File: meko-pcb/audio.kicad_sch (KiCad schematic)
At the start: 29 parts, among them IC4 ES9218PQ, J4 SJ2-35954B-SMT-TR, Y1 ECS-2520SMV-500-GP-TR

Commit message: component selection
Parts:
- IC4: Manufacturer_Part_Number ES9218PQ -> (none); Mfr. No. (none) -> ES9218PQ
- J4: Mfr. No. (none) -> SJ2-35954B-SMT-TR
- R27, R33, R35: Mfr. No. (none) -> CRCW040210K0FKED
- R28, R29: Mfr. No. (none) -> RC0402FR-0747KL
- Y1: Manufacturer_Part_Number ECS-2520SMV-500-GP-TR -> (none); Mfr. No. (none) -> ECS-2520SMV-500-GP-TR
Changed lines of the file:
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@@
+			)
+		)
+		(property "Mfr. No." "RC0402FR-0747KL"
+			(at 146.05 39.37 90)
+			(effects
+				(font
+					(size 1.27 1.27)
+				)
+				(hide yes)
 			)
 		)
@@
 			)
 		)
+		(property "Mfr. No." "CRCW040210K0FKED"
+			(at 21.59 132.08 0)
+			(effects
+				(font
+					(size 1.27 1.27)
+				)
+				(hide yes)
+			)
+		)
 		(pin "2"
 		)
@@
 		(property "Description" "Resistor"
 			(at 146.05 45.72 0)
+			(effects
+				(font
+					(size 1.27 1.27)
+				)
+				(hide yes)
+			)
+		)
+		(property "Mfr. No." "RC0402FR-0747KL"
+			(at 146.05 45.72 90)
 			(effects
 				(font
@@
 			)
 		)
+		(property "Mfr. No." " SJ2-35954B-SMT-TR "
+			(at 60.96 129.54 0)
+			(effects
+				(font
+					(size 1.27 1.27)
+				)
+				(hide yes)
+			)
+		)
 		(pin "R1"
 		)
@@
 			)
 		)
-		(property "Manufacturer_Part_Number" "ECS-2520SMV-500-GP-TR"
-			(at 71.12 680.01 0)
-			(effects
-				(font
-					(size 1.27 1.27)
-				)
-				(justify left top)
-				(hide yes)
-			)
-		)
 		(property "Mouser Part Number" "520-2520SMV-500-GP-T"
 			(at 71.12 780.01 0)
@@
 				)
 				(justify left top)
+				(hide yes)
+			)
+		)
+		(property "Mfr. No." "ECS-2520SMV-500-GP-TR"
+			(at 36.83 85.09 0)
+			(effects
+				(font
+					(size 1.27 1.27)
+				)
 				(hide yes)
 			)
@@
 			)
 		)
-		(property "Manufacturer_Part_Number" "ES9218PQ"
-			(at 149.86 666.04 0)
-			(effects
-				(font
-					(size 1.27 1.27)
-				)
-				(justify left top)
-				(hide yes)
-			)
-		)
 		(property "Mouser Part Number" "460-ES9218PQ"
 			(at 149.86 766.04 0)
@@
 			)
 		)
+		(property "Mfr. No." "ES9218PQ"
+			(at 113.03 83.82 0)
+			(effects
+				(font
+					(size 1.27 1.27)
+				)
+				(hide yes)
+			)
+		)
 		(pin "6"
 		)
@@
 		(property "Description" "Resistor"
 			(at 124.46 36.83 0)
+			(effects
+				(font
+					(size 1.27 1.27)
+				)
+				(hide yes)
+			)
+		)
+		(property "Mfr. No." "CRCW040210K0FKED"
+			(at 124.46 36.83 90)
 			(effects
 				(font
@@
 			(at 35.56 92.71 0)
 			(effects
+				(font
+					(size 1.27 1.27)
+				)
+				(hide yes)
+			)
+		)
+		(property "Mfr. No." "CRCW040210K0FKED"
+			(at 35.56 92.71 0)
+			(effects

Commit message: picked MPNs
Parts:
- C41, C43, C44, C45, C52: MPN (none) -> CL05A105KO5NNNC
- C42: MPN (none) -> CL10A226MQ8NRNC
- C46, C47, C48, C49, C50: MPN (none) -> CL05A475KP5NRNC
- C51: MPN (none) -> CL05A225KO5NQNC
- C53, C54, C55, C56: MPN (none) -> CL05B222KB5NNNC
- D10, D11, D12, D9: MPN (none) -> CD0201-T2.0LC; Mfr. No. CD0201-T2.0LC -> (none)
- IC4: MPN (none) -> ES9218PQ; Mfr. No. ES9218PQ -> (none); Mouser Part Number 460-ES9218PQ -> (none); Mouser Price/Stock https://www.mouser.co.uk/ProductDetail/ESS-Technology/ES921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 -> (none)
- J4: MPN (none) -> SJ2-35954B-SMT-TR; Mfr. No. SJ2-35954B-SMT-TR -> (none)
- R27, R33, R35: MPN (none) -> CRCW040210K0FKED; Mfr. No. CRCW040210K0FKED -> (none)
- R28, R29: MPN (none) -> RC0402FR-0747KL; Mfr. No. RC0402FR-0747KL -> (none)
- Y1: MPN (none) -> ECS-2520SMV-500-GP-TR; Mfr. No. ECS-2520SMV-500-GP-TR -> (none); Mouser Part Number 520-2520SMV-500-GP-T -> (none); Mouser Price/Stock https://www.mouser.co.uk/ProductDetail/ECS/ECS-2520SMV-500-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 -> (none)
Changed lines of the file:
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@@
 			)
 		)
+		(property "MPN" "CL05B222KB5NNNC"
+			(at 168.91 99.06 90)
+			(effects
+				(font
+					(size 1.27 1.27)
+				)
+				(hide yes)
+			)
+		)
 		(pin "1"
 		)
@@
 			)
 		)
+		(property "MPN" "CL05B222KB5NNNC"
+			(at 104.14 106.68 0)
+			(effects
+				(font
+					(size 1.27 1.27)
+				)
+				(hide yes)
+			)
+		)
 		(pin "1"
 		)
@@
 			)
 		)
-		(property "Mfr. No." "RC0402FR-0747KL"
+		(property "MPN" "RC0402FR-0747KL"
 			(at 146.05 39.37 90)
 			(effects
@@
 			)
 		)
-		(property "Mfr. No." " CD0201-T2.0LC "
+		(property "MPN" " CD0201-T2.0LC "
 			(at 39.37 147.32 90)
 			(effects
@@
 			)
 		)
+		(property "MPN" "CL05A105KO5NNNC"
+			(at 128.27 142.24 0)
+			(effects
+				(font
+					(size 1.27 1.27)
+				)
+				(hide yes)
+			)
+		)
 		(pin "1"
 		)
@@
 			)
 		)
+		(property "MPN" "CL05A105KO5NNNC"
+			(at 45.72 26.67 0)
+			(effects
+				(font
+					(size 1.27 1.27)
+				)
+				(hide yes)
+			)
+		)
 		(pin "1"
 		)
@@
 			)
 		)
+		(property "MPN" "CL05A105KO5NNNC"
+			(at 168.91 73.66 90)
+			(effects
+				(font
+					(size 1.27 1.27)
+				)
+				(hide yes)
+			)
+		)
 		(pin "1"
 		)
@@
 			)
 		)
+		(property "MPN" "CL05A105KO5NNNC"
+			(at 58.42 26.67 0)
+			(effects
+				(font
+					(size 1.27 1.27)
+				)
+				(hide yes)
+			)
+		)
 		(pin "1"
 		)
@@
 			)
 		)
-		(property "Mfr. No." "CRCW040210K0FKED"
+		(property "MPN" "CRCW040210K0FKED"
 			(at 21.59 132.08 0)
 			(effects
@@
 			)
 		)
-		(property "Mfr. No." "RC0402FR-0747KL"
+		(property "MPN" "RC0402FR-0747KL"
 			(at 146.05 45.72 90)
 			(effects
@@
 			)
 		)
+		(property "MPN" "CL05A105KO5NNNC"
+			(at 147.32 25.4 90)
+			(effects
+				(font
+					(size 1.27 1.27)
+				)
+				(hide yes)
+			)
+		)
 		(pin "2"
 		)
@@
 			)
 		)
+		(property "MPN" "CL05B222KB5NNNC"
+			(at 166.37 106.68 0)
+			(effects
+				(font
+					(size 1.27 1.27)
+				)
+				(hide yes)
+			)
+		)
 		(pin "1"
 		)
@@
 			)
 		)
+		(property "MPN" "CL05A475KP5NRNC"
+			(at 45.72 52.07 0)
+			(effects
+				(font
+					(size 1.27 1.27)
+				)
+				(hide yes)
+			)
+		)
 		(pin "1"
 		)
@@
 			)
 		)
-		(property "Mfr. No." " SJ2-35954B-SMT-TR "
+		(property "MPN" " SJ2-35954B-SMT-TR "
 			(at 60.96 129.54 0)
 			(effects
@@
 			)
 		)
+		(property "MPN" "CL05A475KP5NRNC"
+			(at 21.59 52.07 0)
+			(effects
+				(font
+					(size 1.27 1.27)
+				)
+				(hide yes)
+			)
+		)
 		(pin "1"
 		)
@@
 			)
 		)
-		(property "Mouser Part Number" "520-2520SMV-500-GP-T"
-			(at 71.12 780.01 0)
-			(effects
-				(font
-					(size 1.27 1.27)
-				)
-				(justify left top)
-				(hide yes)
-			)
-		)
-		(property "Mouser Price/Stock" "https://www.mouser.co.uk/ProductDetail/ECS/ECS-2520SMV-500-GP-TR?qs=XeJtXLiO41S1fNQUYV715g%3D%3D"
-			(at 71.12 880.01 0)
-			(effects
-				(font
-					(size 1.27 1.27)
-				)
-				(justify left top)
-				(hide yes)
-			)
-		)
 		(property "Arrow Part Number" "ECS-2520SMV-500-GP-TR"
 			(at 71.12 980.01 0)
@@
 			)
 		)
-		(property "Mfr. No." "ECS-2520SMV-500-GP-TR"
+		(property "MPN" "ECS-2520SMV-500-GP-TR"
 			(at 36.83 85.09 0)
 			(effects
@@
 			)
 		)
-		(property "Mouser Part Number" "460-ES9218PQ"
-			(at 149.86 766.04 0)
-			(effects
-				(font
-					(size 1.27 1.27)
-				)
-				(justify left top)
-				(hide yes)
-			)
-		)
-		(property "Mouser Price/Stock" "https://www.mouser.co.uk/ProductDetail/ESS-Technology/ES9218PQ?qs=sPbYRqrBIVkIKXrxpjKBFg%3D%3D"
-			(at 149.86 866.04 0)
-			(effects
-				(font
-					(size 1.27 1.27)
-				)
-				(justify left top)
-				(hide yes)
-			)
-		)
 		(property "Arrow Part Number" ""
 			(at 149.86 966.04 0)
@@
 			)
 		)
-		(property "Mfr. No." "ES9218PQ"
+		(property "MPN" "ES9218PQ"
 			(at 113.03 83.82 0)
 			(effects
@@
 			)
 		)
+		(property "MPN" "CL05A475KP5NRNC"
+			(at 57.15 52.07 0)
+			(effects
+				(font
+					(size 1.27 1.27)
+				)
+				(hide yes)
+			)
+		)
 		(pin "1"
 		)
@@
 			)
 		)
-		(property "Mfr. No." "CRCW040210K0FKED"
+		(property "MPN" "CRCW040210K0FKED"
 			(at 124.46 36.83 90)
 			(effects
@@
 			)
 		)
+		(property "MPN" "CL05A225KO5NQNC"
+			(at 168.91 68.58 90)
+			(effects
+				(font
+					(size 1.27 1.27)
+				)
+				(hide yes)
+			)
+		)
 		(pin "1"
 		)
@@
 			)
 		)
-		(property "Mfr. No." " CD0201-T2.0LC "
+		(property "MPN" " CD0201-T2.0LC "
 			(at 44.45 147.32 90)
 			(effects
@@
 			)
 		)
-		(property "Mfr. No." " CD0201-T2.0LC "
+		(property "MPN" " CD0201-T2.0LC "
 			(at 49.53 147.32 90)
 			(effects
@@
 			)
 		)
-		(property "Mfr. No." "CRCW040210K0FKED"
+		(property "MPN" "CRCW040210K0FKED"
 			(at 35.56 92.71 0)
 			(effects
@@
 			)
 		)
+		(property "MPN" "CL05A475KP5NRNC"
+			(at 71.12 26.67 0)
+			(effects
+				(font
+					(size 1.27 1.27)
+				)
+				(hide yes)
+			)
+		)
 		(pin "1"
 		)
@@
 			)
 		)
+		(property "MPN" "CL05B222KB5NNNC"
+			(at 95.25 99.06 90)
+			(effects
+				(font
+					(size 1.27 1.27)
+				)
+				(hide yes)
+			)
+		)
 		(pin "1"
 		)
@@
 			)
 		)
-		(property "Mfr. No." " CD0201-T2.0LC "
+		(property "MPN" " CD0201-T2.0LC "
 			(at 54.61 147.32 90)
 			(effects
@@
 			)
 		)
+		(property "MPN" "CL10A226MQ8NRNC"
+			(at 121.92 142.24 0)
+			(effects
+				(font
+					(size 1.27 1.27)
+				)
+				(hide yes)
+			)
+		)
 		(pin "1"
 		)
@@
 			(at 34.29 52.07 0)
 			(effects
+				(font
+					(size 1.27 1.27)
+				)
+				(hide yes)
+			)
+		)
+		(property "MPN" "CL05A475KP5NRNC"
+			(at 34.29 52.07 0)
+			(effects

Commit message: small changes, readme updates
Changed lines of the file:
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@@
 		(dnp no)
 		(property "Reference" "IC4"
-			(at 112.522 72.136 0)
+			(at 99.06 67.31 0)
 			(effects
 				(font
@@
 		)
 		(property "Value" "ES9218PQ"
-			(at 112.522 74.676 0)
+			(at 99.06 69.85 0)
 			(effects
 				(font

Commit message: readme updates, removed unused fileds form kicad
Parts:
- IC4: Height 0.8 -> (none); Manufacturer_Name ESS Technology -> (none)
- Y1: Arrow Part Number ECS-2520SMV-500-GP-TR -> (none); Arrow Price/Stock https://www.arrow.com/en/products/ecs-2520smv-500-gp-tr/ecs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 -> (none); Height 0.9 -> (none); Manufacturer_Name ECS -> (none)
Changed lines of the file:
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@@
-			)
-		)
-		(property "Height" "0.9"
-			(at 71.12 480.01 0)
-			(effects
-				(font
-					(size 1.27 1.27)
-				)
-				(justify left top)
-				(hide yes)
-			)
-		)
-		(property "Manufacturer_Name" "ECS"
-			(at 71.12 580.01 0)
-			(effects
-				(font
-					(size 1.27 1.27)
-				)
-				(justify left top)
-				(hide yes)
-			)
-		)
-		(property "Arrow Part Number" "ECS-2520SMV-500-GP-TR"
-			(at 71.12 980.01 0)
-			(effects
-				(font
-					(size 1.27 1.27)
-				)
-				(justify left top)
-				(hide yes)
-			)
-		)
-		(property "Arrow Price/Stock" "https://www.arrow.com/en/products/ecs-2520smv-500-gp-tr/ecs-international?region=nac"
-			(at 71.12 1080.01 0)
-			(effects
-				(font
-					(size 1.27 1.27)
-				)
-				(justify left top)
-				(hide yes)
 			)
 		)
@@
 				(hide yes)
 			)
-		)
-		(property "Height" "0.8"
-			(at 149.86 466.04 0)
-			(effects
-				(font
-					(size 1.27 1.27)
-				)
-				(justify left top)
-				(hide yes)
-			)
-		)
-		(property "Manufacturer_Name" "ESS Technology"
-			(at 149.86 566.04 0)
-			(effects
-				(font
-					(size 1.27 1.27)
-				)
-				(justify left top)
-				(hide yes)
-			)
-		)
-		(property "Arrow Part Number" ""
-			(at 149.86 966.04 0)
-			(effects
-				(font
-					(size 1.27 1.27)
-				)
-				(justify left top)
-				(hide yes)
-			)
-		)
-		(property "Arrow Price/Stock" ""
-			(at 149.86 1066.04 0)
-			(effects
-				(font
-					(size 1.27 1.27)
-				)
-				(justify left top)
-				(hide yes)
-			)

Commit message: new blender scene
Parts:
- C53, C54, C55, C56: MPN CL05B222KB5NNNC -> GRM1555C1H222JA01J
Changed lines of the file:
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@@
 			)
 		)
-		(property "MPN" "CL05B222KB5NNNC"
+		(property "MPN" "GRM1555C1H222JA01J"
 			(at 168.91 99.06 90)
 			(effects
@@
 			)
 		)
-		(property "MPN" "CL05B222KB5NNNC"
+		(property "MPN" "GRM1555C1H222JA01J"
 			(at 104.14 106.68 0)
 			(effects
@@
 			)
 		)
-		(property "MPN" "CL05B222KB5NNNC"
+		(property "MPN" "GRM1555C1H222JA01J"
 			(at 166.37 106.68 0)
 			(effects
@@
 			)
 		)
-		(property "MPN" "CL05B222KB5NNNC"
+		(property "MPN" "GRM1555C1H222JA01J"
 			(at 95.25 99.06 90)
 			(effects

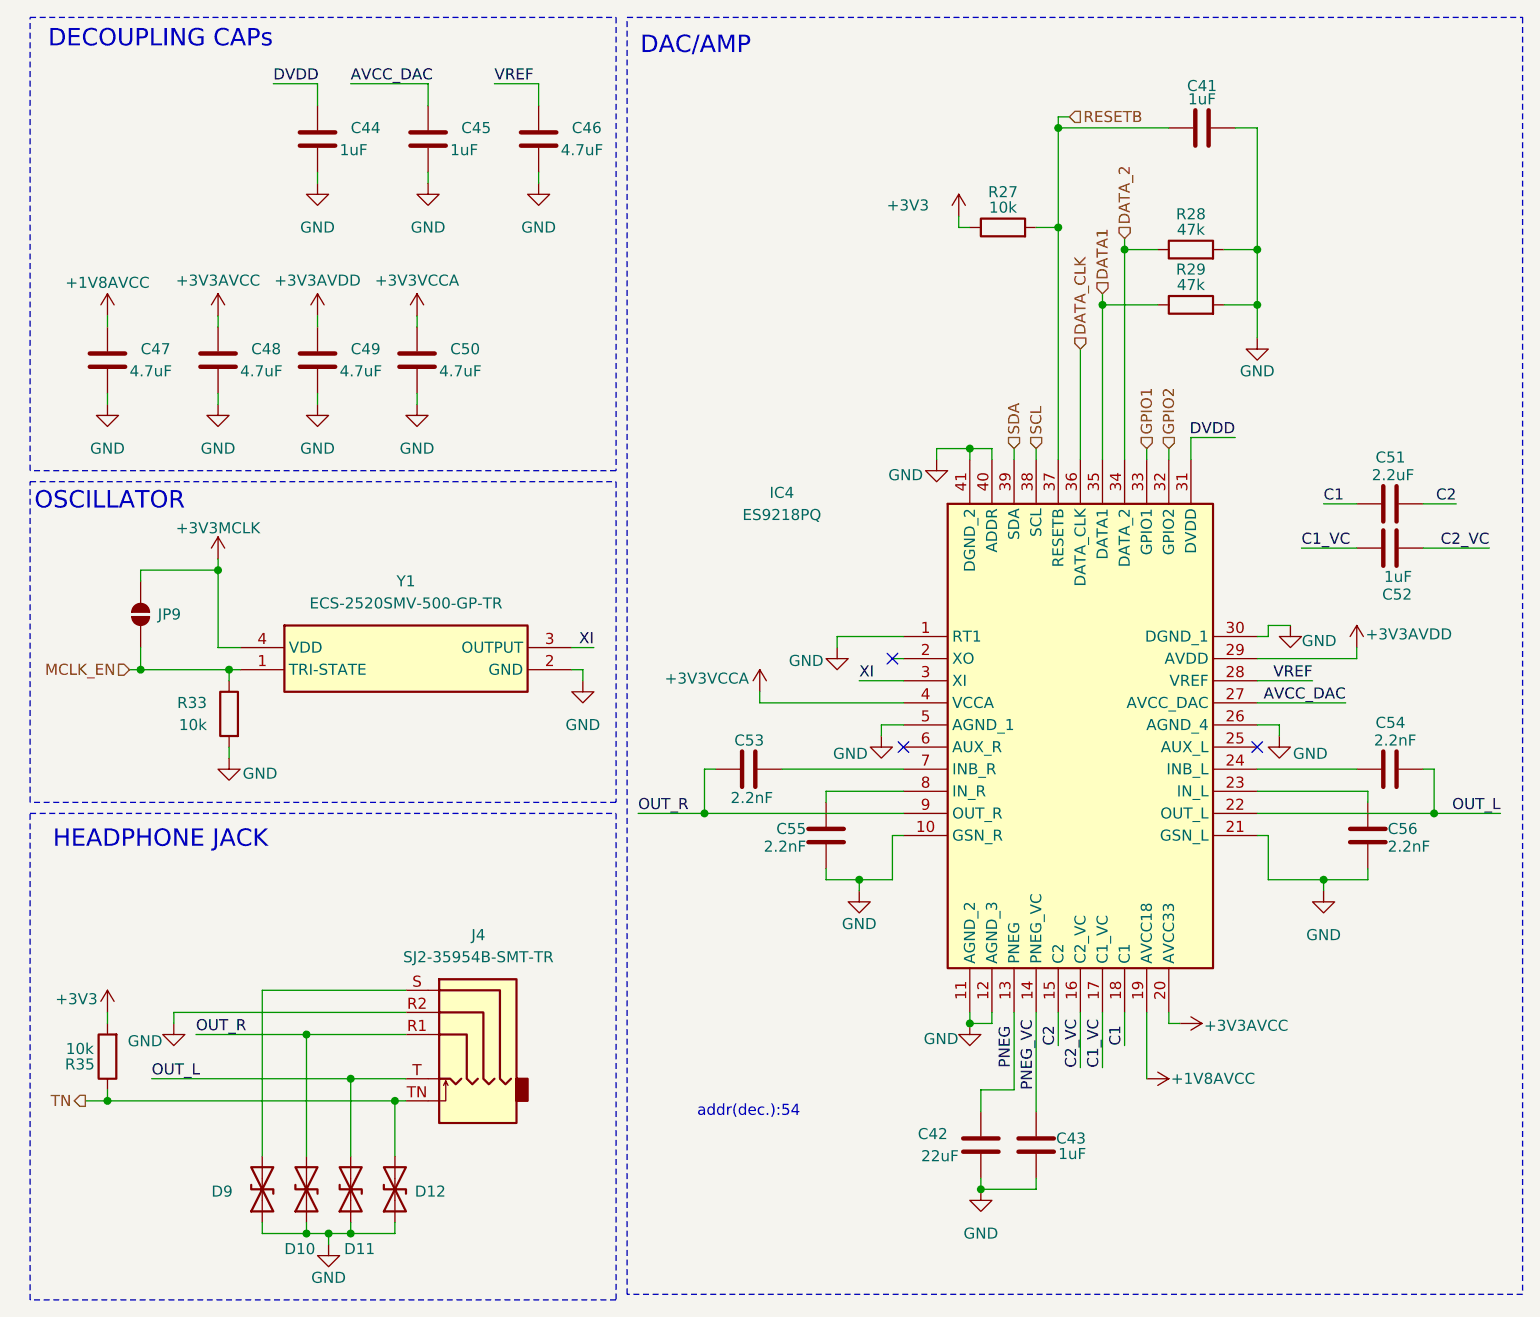
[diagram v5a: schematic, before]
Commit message: started to implement npm1300
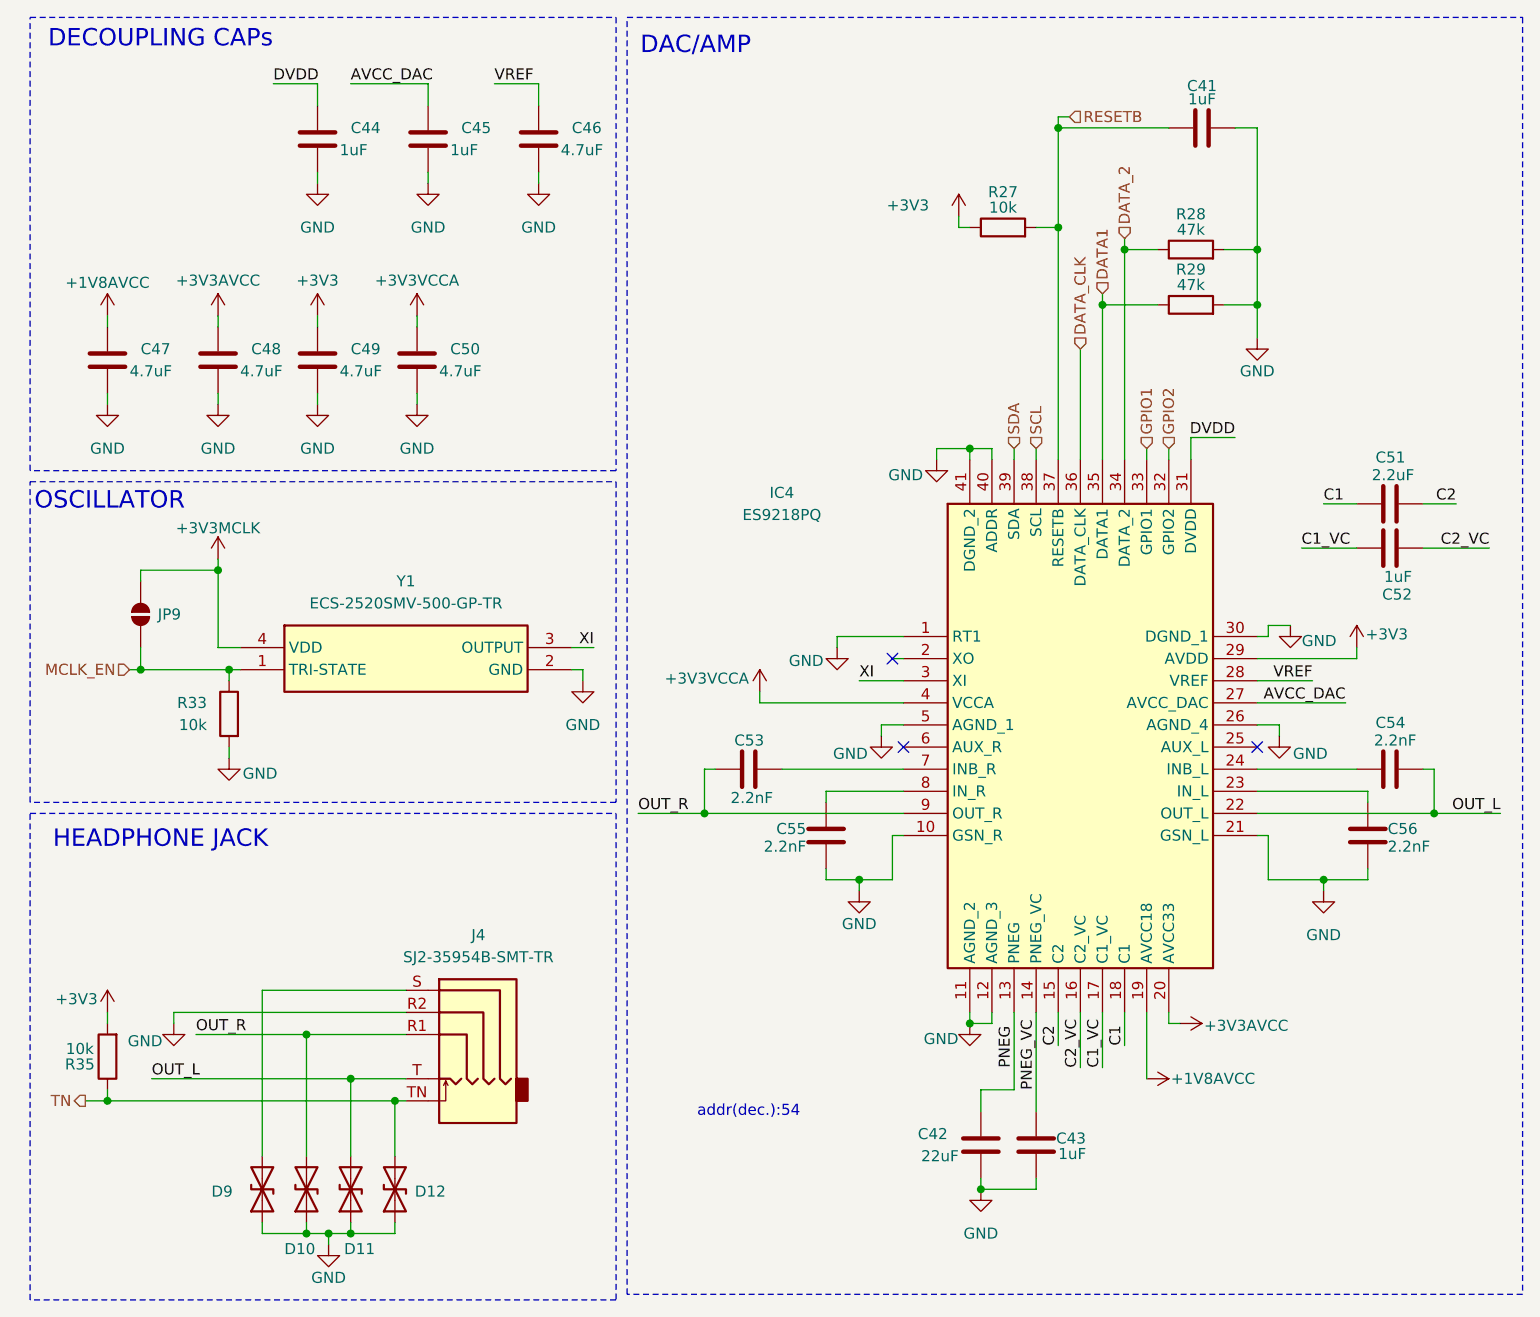
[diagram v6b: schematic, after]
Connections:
- net +3V3AVDD is gone; now on net +3V3: C49.1, IC4.29 (AVDD)
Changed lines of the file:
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@@
 			)
 		)
-		(property "Value" "+3V3AVDD"
+		(property "Value" "+3V3"
 			(at 166.116 83.566 0)
 			(effects
@@
 			)
 		)
-		(property "Value" "+3V3AVDD"
+		(property "Value" "+3V3"
 			(at 45.72 42.926 0)
 			(effects

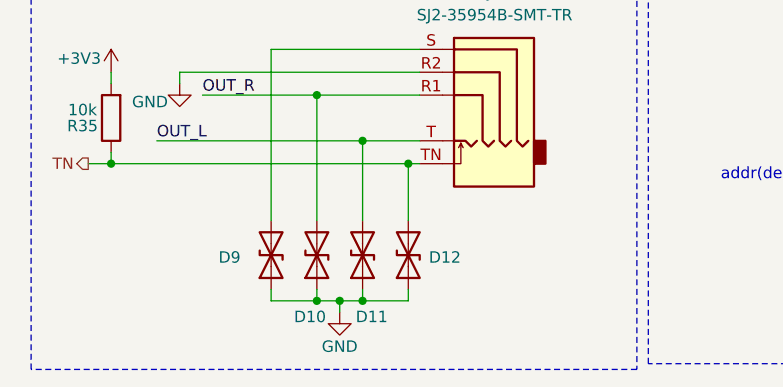
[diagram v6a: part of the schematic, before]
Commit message: added new ldos, made improvements to the schematic
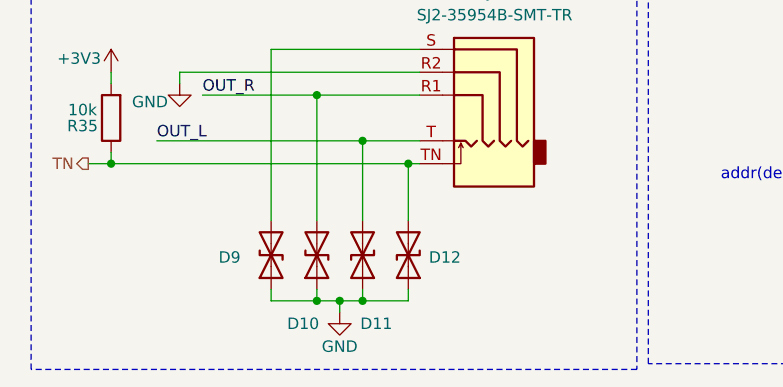
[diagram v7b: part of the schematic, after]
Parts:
- D10, D11, D12, D9: footprint CD0201-T2.0LC:CD0201T20LC -> (none)
